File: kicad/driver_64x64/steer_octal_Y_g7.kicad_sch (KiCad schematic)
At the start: 66 parts

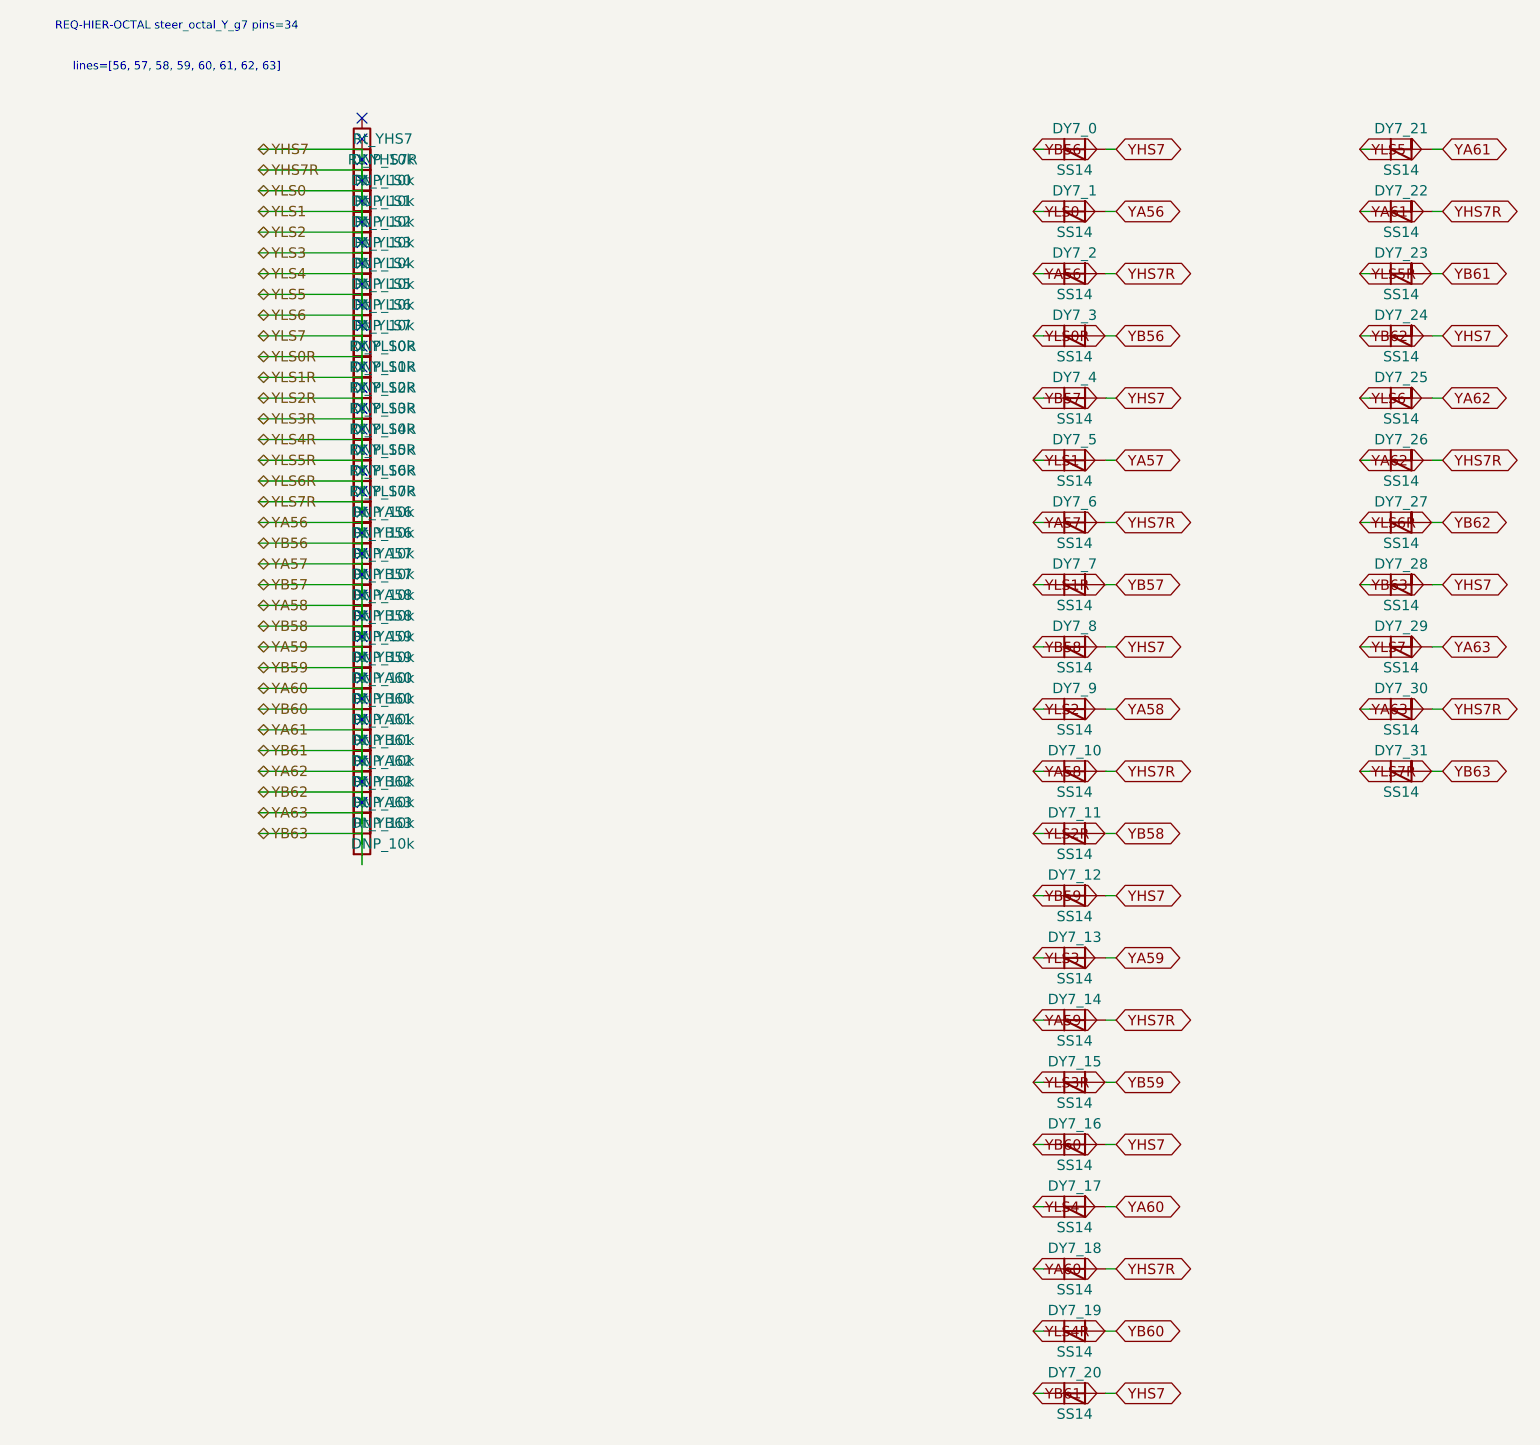
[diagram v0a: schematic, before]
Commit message: logical seperation into host and multiple decode/drive/steering boards
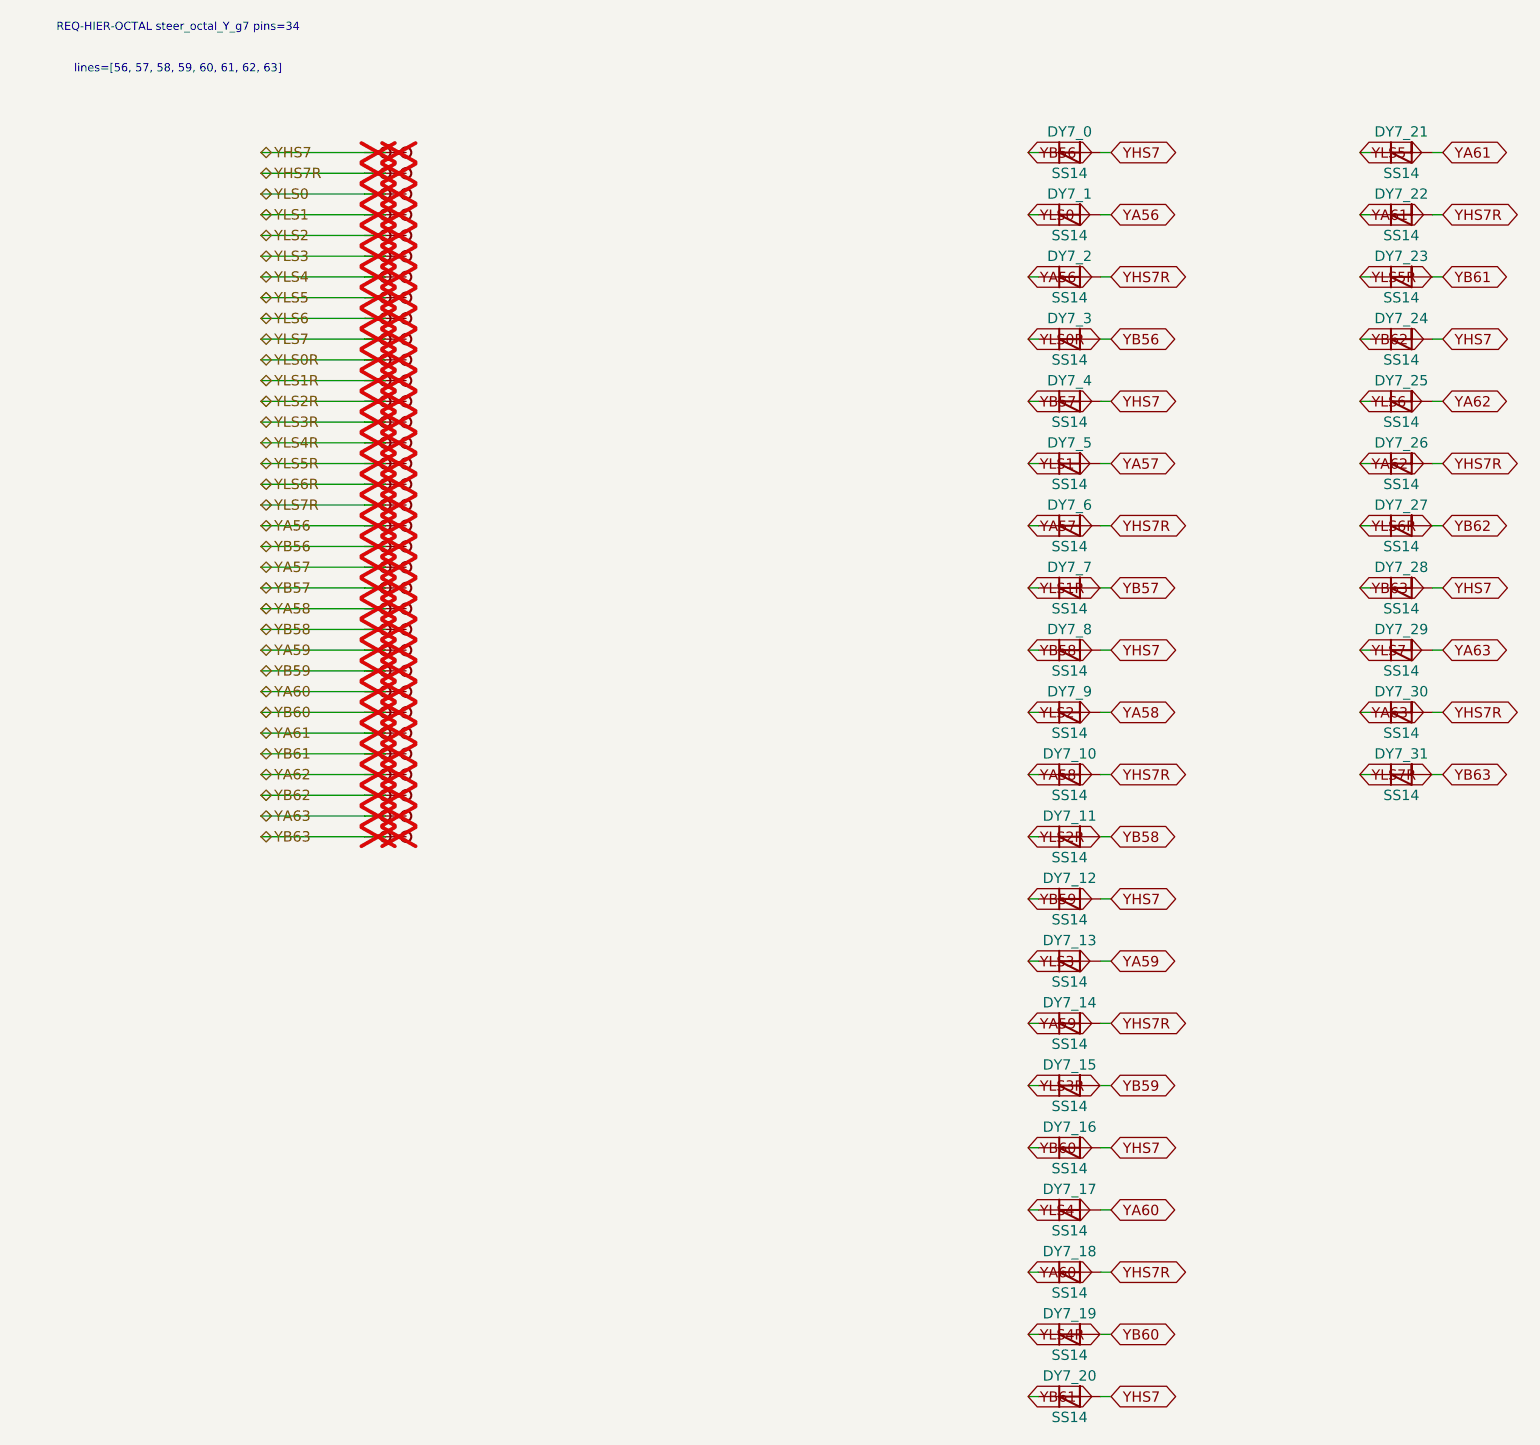
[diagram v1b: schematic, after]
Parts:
- removed Rt_YA56, Rt_YA57, Rt_YA58, Rt_YA59, Rt_YA60, Rt_YA61, Rt_YA62, Rt_YA63, Rt_YB56, Rt_YB57, Rt_YB58, Rt_YB59, Rt_YB60, Rt_YB61, Rt_YB62, Rt_YB63, Rt_YHS7, Rt_YHS7R, Rt_YLS0, Rt_YLS0R, Rt_YLS1, Rt_YLS1R, Rt_YLS2, Rt_YLS2R, Rt_YLS3, Rt_YLS3R, Rt_YLS4, Rt_YLS4R, Rt_YLS5, Rt_YLS5R, Rt_YLS6, Rt_YLS6R, Rt_YLS7, Rt_YLS7R: DNP_10k, symbol Device:R
- added TP_YA56, TP_YA56b, TP_YA57, TP_YA57b, TP_YA58, TP_YA58b, TP_YA59, TP_YA59b, TP_YA60, TP_YA60b, TP_YA61, TP_YA61b, TP_YA62, TP_YA62b, TP_YA63, TP_YA63b, TP_YB56, TP_YB56b, TP_YB57, TP_YB57b, TP_YB58, TP_YB58b, TP_YB59, TP_YB59b, TP_YB60, TP_YB60b, TP_YB61, TP_YB61b, TP_YB62, TP_YB62b, TP_YB63, TP_YB63b, TP_YHS7, TP_YHS7R, TP_YHS7Rb, TP_YHS7b, TP_YLS0, TP_YLS0R, TP_YLS0Rb, TP_YLS0b, TP_YLS1, TP_YLS1R, TP_YLS1Rb, TP_YLS1b, TP_YLS2, TP_YLS2R, TP_YLS2Rb, TP_YLS2b, TP_YLS3, TP_YLS3R, TP_YLS3Rb, TP_YLS3b, TP_YLS4, TP_YLS4R, TP_YLS4Rb, TP_YLS4b, TP_YLS5, TP_YLS5R, TP_YLS5Rb, TP_YLS5b, TP_YLS6, TP_YLS6R, TP_YLS6Rb, TP_YLS6b, TP_YLS7, TP_YLS7R, TP_YLS7Rb, TP_YLS7b: Stub, symbol CMR:Stub
- DY7_0, DY7_1, DY7_10, DY7_11, DY7_12, DY7_13, DY7_14, DY7_15, DY7_16, DY7_17, DY7_18, DY7_19, DY7_2, DY7_20, DY7_21, DY7_22, DY7_23, DY7_24, DY7_25, DY7_26, DY7_27, DY7_28, DY7_29, DY7_3, DY7_30, DY7_31, DY7_4, DY7_5, DY7_6, DY7_7, DY7_8, DY7_9: symbol Device:D_Schottky -> CMR:D_Schottky
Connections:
- net YA56: now also TP_YA56.1, TP_YA56b.1; no longer DY7_0.1 (K), DY7_0.2 (A), DY7_1.1 (K), DY7_10.1 (K), DY7_10.2 (A), DY7_11.1 (K), DY7_11.2 (A), DY7_12.1 (K), DY7_12.2 (A), DY7_13.1 (K), DY7_13.2 (A), DY7_14.1 (K), DY7_14.2 (A), DY7_15.1 (K), DY7_15.2 (A), DY7_16.1 (K), DY7_16.2 (A), DY7_17.1 (K), DY7_17.2 (A), DY7_18.1 (K), DY7_18.2 (A), DY7_19.1 (K), DY7_19.2 (A), DY7_2.2 (A), DY7_20.1 (K), DY7_20.2 (A), DY7_21.1 (K), DY7_21.2 (A), DY7_22.1 (K), DY7_22.2 (A), DY7_23.1 (K), DY7_23.2 (A), DY7_24.1 (K), DY7_24.2 (A), DY7_25.1 (K), DY7_25.2 (A), DY7_26.1 (K), DY7_26.2 (A), DY7_27.1 (K), DY7_27.2 (A), DY7_28.1 (K), DY7_28.2 (A), DY7_29.1 (K), DY7_29.2 (A), DY7_3.1 (K), DY7_3.2 (A), DY7_30.1 (K), DY7_30.2 (A), DY7_31.1 (K), DY7_31.2 (A), DY7_4.1 (K), DY7_4.2 (A), DY7_5.1 (K), DY7_5.2 (A), DY7_6.1 (K), DY7_6.2 (A), DY7_7.1 (K), DY7_7.2 (A), DY7_8.1 (K), DY7_8.2 (A), DY7_9.1 (K), DY7_9.2 (A)
- new net YA57: DY7_5.2 (A), DY7_6.1 (K), TP_YA57.1, TP_YA57b.1
- new net YA58: DY7_10.1 (K), DY7_9.2 (A), TP_YA58.1, TP_YA58b.1
- new net YA59: DY7_13.2 (A), DY7_14.1 (K), TP_YA59.1, TP_YA59b.1
- new net YA60: DY7_17.2 (A), DY7_18.1 (K), TP_YA60.1, TP_YA60b.1
- new net YA61: DY7_21.2 (A), DY7_22.1 (K), TP_YA61.1, TP_YA61b.1
- new net YA62: DY7_25.2 (A), DY7_26.1 (K), TP_YA62.1, TP_YA62b.1
- new net YA63: DY7_29.2 (A), DY7_30.1 (K), TP_YA63.1, TP_YA63b.1
- new net YB56: DY7_0.1 (K), DY7_3.2 (A), TP_YB56.1, TP_YB56b.1
- new net YB57: DY7_4.1 (K), DY7_7.2 (A), TP_YB57.1, TP_YB57b.1
- new net YB58: DY7_11.2 (A), DY7_8.1 (K), TP_YB58.1, TP_YB58b.1
- new net YB59: DY7_12.1 (K), DY7_15.2 (A), TP_YB59.1, TP_YB59b.1
- new net YB60: DY7_16.1 (K), DY7_19.2 (A), TP_YB60.1, TP_YB60b.1
- new net YB61: DY7_20.1 (K), DY7_23.2 (A), TP_YB61.1, TP_YB61b.1
- new net YB62: DY7_24.1 (K), DY7_27.2 (A), TP_YB62.1, TP_YB62b.1
- new net YB63: DY7_28.1 (K), DY7_31.2 (A), TP_YB63.1, TP_YB63b.1
- new net YHS7: DY7_0.2 (A), DY7_12.2 (A), DY7_16.2 (A), DY7_20.2 (A), DY7_24.2 (A), DY7_28.2 (A), DY7_4.2 (A), DY7_8.2 (A), TP_YHS7.1, TP_YHS7b.1
- new net YHS7R: DY7_10.2 (A), DY7_14.2 (A), DY7_18.2 (A), DY7_2.2 (A), DY7_22.2 (A), DY7_26.2 (A), DY7_30.2 (A), DY7_6.2 (A), TP_YHS7R.1, TP_YHS7Rb.1
- new net YLS0: DY7_1.1 (K), TP_YLS0.1, TP_YLS0b.1
- new net YLS0R: DY7_3.1 (K), TP_YLS0R.1, TP_YLS0Rb.1
- new net YLS1: DY7_5.1 (K), TP_YLS1.1, TP_YLS1b.1
- new net YLS1R: DY7_7.1 (K), TP_YLS1R.1, TP_YLS1Rb.1
- new net YLS2: DY7_9.1 (K), TP_YLS2.1, TP_YLS2b.1
- new net YLS2R: DY7_11.1 (K), TP_YLS2R.1, TP_YLS2Rb.1
- new net YLS3: DY7_13.1 (K), TP_YLS3.1, TP_YLS3b.1
- new net YLS3R: DY7_15.1 (K), TP_YLS3R.1, TP_YLS3Rb.1
- new net YLS4: DY7_17.1 (K), TP_YLS4.1, TP_YLS4b.1
- new net YLS4R: DY7_19.1 (K), TP_YLS4R.1, TP_YLS4Rb.1
- new net YLS5: DY7_21.1 (K), TP_YLS5.1, TP_YLS5b.1
- new net YLS5R: DY7_23.1 (K), TP_YLS5R.1, TP_YLS5Rb.1
- new net YLS6: DY7_25.1 (K), TP_YLS6.1, TP_YLS6b.1
- new net YLS6R: DY7_27.1 (K), TP_YLS6R.1, TP_YLS6Rb.1
- new net YLS7: DY7_29.1 (K), TP_YLS7.1, TP_YLS7b.1
- new net YLS7R: DY7_31.1 (K), TP_YLS7R.1, TP_YLS7Rb.1
- no-connect marks 34 -> 0
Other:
- moved on the sheet: DY7_0, DY7_1, DY7_10, DY7_11, DY7_12, DY7_13, DY7_14, DY7_15, DY7_16, DY7_17, DY7_18, DY7_19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
